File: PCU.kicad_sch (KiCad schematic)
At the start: 7 parts, among them U4 EPC2152, Y1 AMDLA4020S-220MT

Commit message: lastest
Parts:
- added J11: Screw_Terminal_01x04, TerminalBlock_Phoenix:TerminalBlock_Phoenix_MKDS-1,5-4-5.08_1x04_P5.08mm_Horizontal, symbol Connector:Screw_Terminal_01x04
- added TP2: 12Vin_buck, TestPoint:TestPoint_Pad_D2.0mm, symbol Connector:TestPoint_Probe
- added TP5: PWM_H, TestPoint:TestPoint_Pad_D2.0mm, symbol Connector:TestPoint_Probe
- added TP6: PWM_L, TestPoint:TestPoint_Pad_D2.0mm, symbol Connector:TestPoint_Probe
- added TP7: Buck_out, TestPoint:TestPoint_Pad_D2.0mm, symbol Connector:TestPoint_2Pole
- C12: footprint CAPC3216X180N -> PULSE_Library:CAPC3216X180N
- C7, C8, C9: footprint (none) -> Capacitor_SMD:C_0201_0603Metric
- L2: footprint (none) -> Inductor_SMD:L_10.4x10.4_H4.8
- U4: footprint EPC_FETs:D0122 -> PULSE_Library:VREG_EPC2152ENGRT
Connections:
- net V_in_12V: now also J11.1 (Pin_1), TP2.1
- net V_out: now also J11.2 (Pin_2), TP7.1
- net pwm_H: now also TP5.1
- net pwm_L: now also TP6.1
- net at C12.1, C9.2, U4.12 (Vss): now also TP7.2
- net at C8.1, U4.1 (Vdd12F): now also J11.3 (Pin_3)
- net gnd renamed GROUND
- new net GND: J11.4 (Pin_4)
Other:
- moved on the sheet: C7

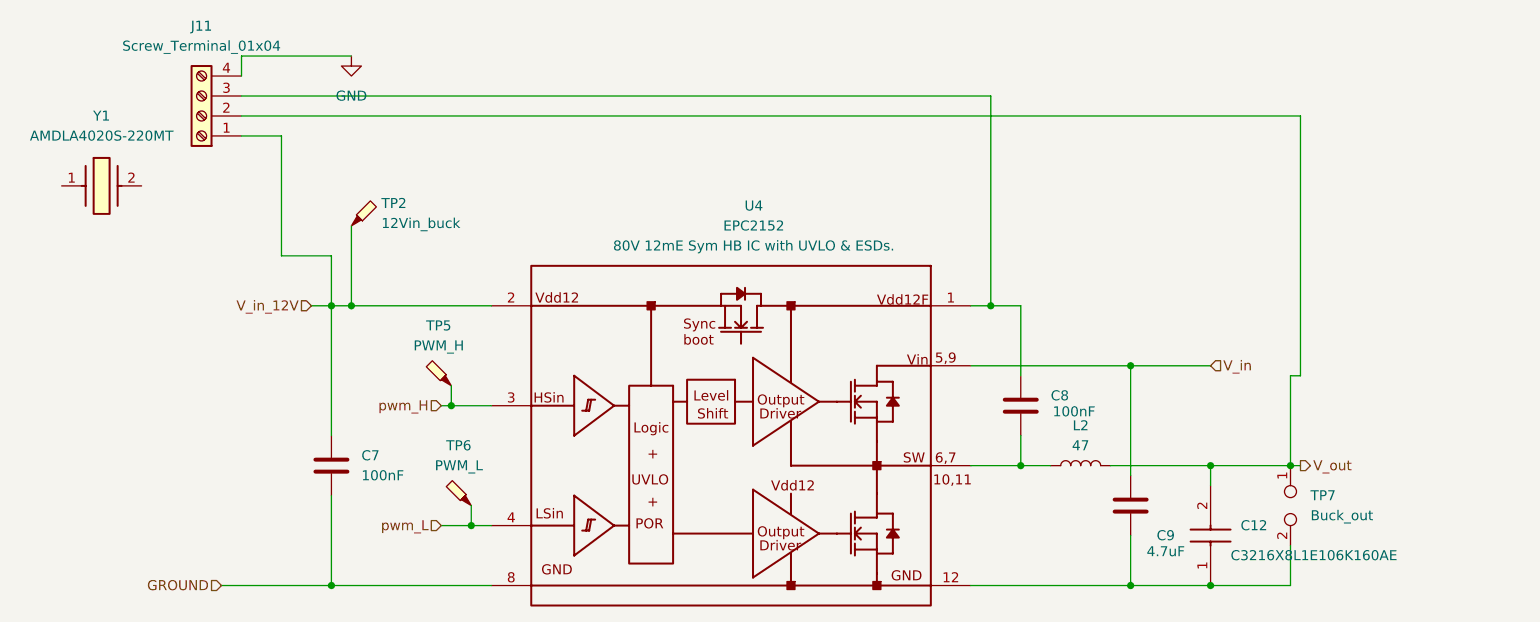
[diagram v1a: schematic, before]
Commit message: fixed LDO
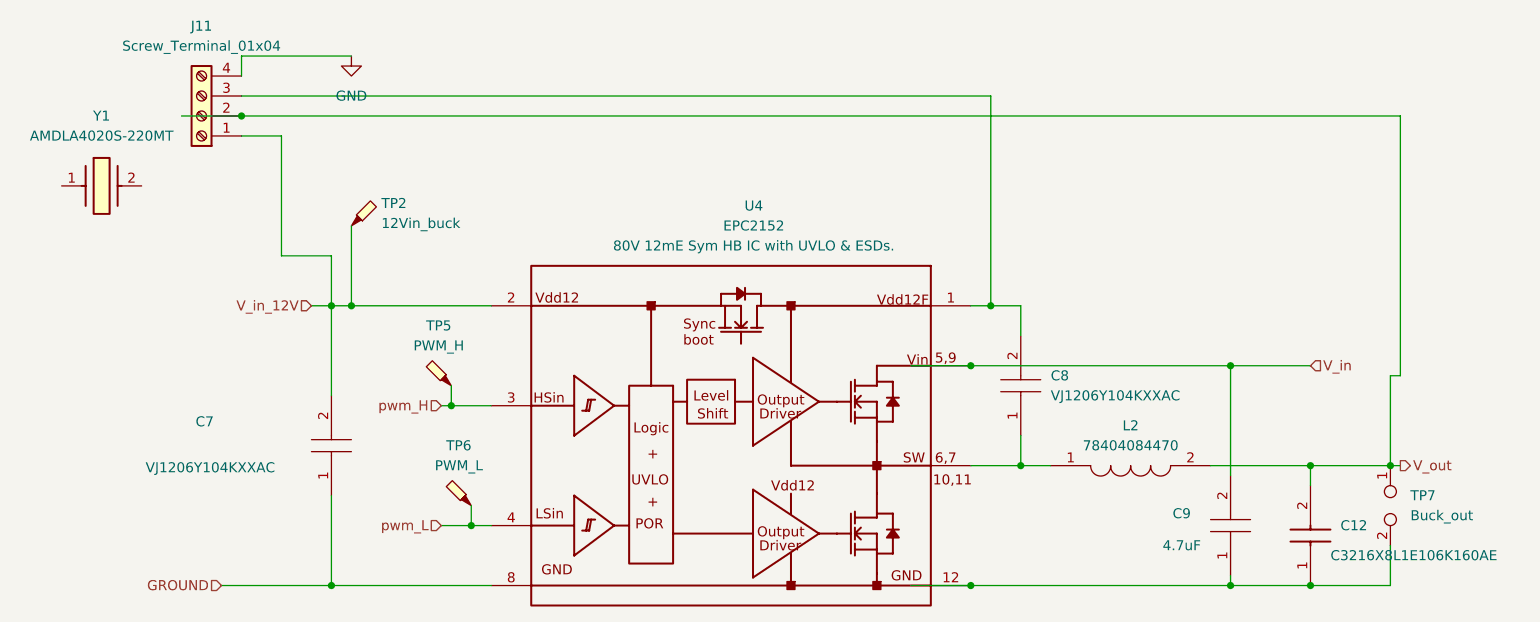
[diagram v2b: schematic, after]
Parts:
- removed C7, C8: 100nF, Capacitor_SMD:C_0201_0603Metric, symbol SamacSys_Parts:C
- removed C9: 4.7uF, Capacitor_SMD:C_0201_0603Metric, symbol SamacSys_Parts:C
- removed L2: 47, Inductor_SMD:L_10.4x10.4_H4.8, symbol SamacSys_Parts:L
- added C7, C8: VJ1206Y104KXXAC, CAPC3216X170N, symbol PULSE_Library:VJ1206Y104KXXAC
- added C9: 4.7uF, PULSE_Library:CAPC3216X180N, symbol PULSE_Library:C3216X8R1E475M160AE
- added L2: 78404084470, 78404084470, symbol PULSE_Library:78404084470
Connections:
- net GROUND: now also C7.1
- net V_in: now also C9.2
- net V_in_12V: now also C7.2
- net V_out: now also L2.2
- net at C12.1, TP7.2, U4.12 (Vss): now also C9.1
- net at J11.3 (Pin_3), U4.1 (Vdd12F): now also C8.2
- net at U4.10 (SW), U4.11 (SW), U4.6 (SW)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: now also C8.1, L2.1
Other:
- moved on the sheet: C12, TP7
